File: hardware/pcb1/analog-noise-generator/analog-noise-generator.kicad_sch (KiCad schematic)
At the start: 83 parts, among them J1 USB_C_Receptacle_USB2.0, J2 Conn_01x03_Pin, J3 PJ-211A, J4 PJ-211A, J5 Conn_01x04_Pin, J6 Conn_01x04_Pin, J7 Conn_01x02_Pin, J9 Conn_02x04_Odd_Even, U1 STM32F072CBTx, U2 USBLC6-2SC6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

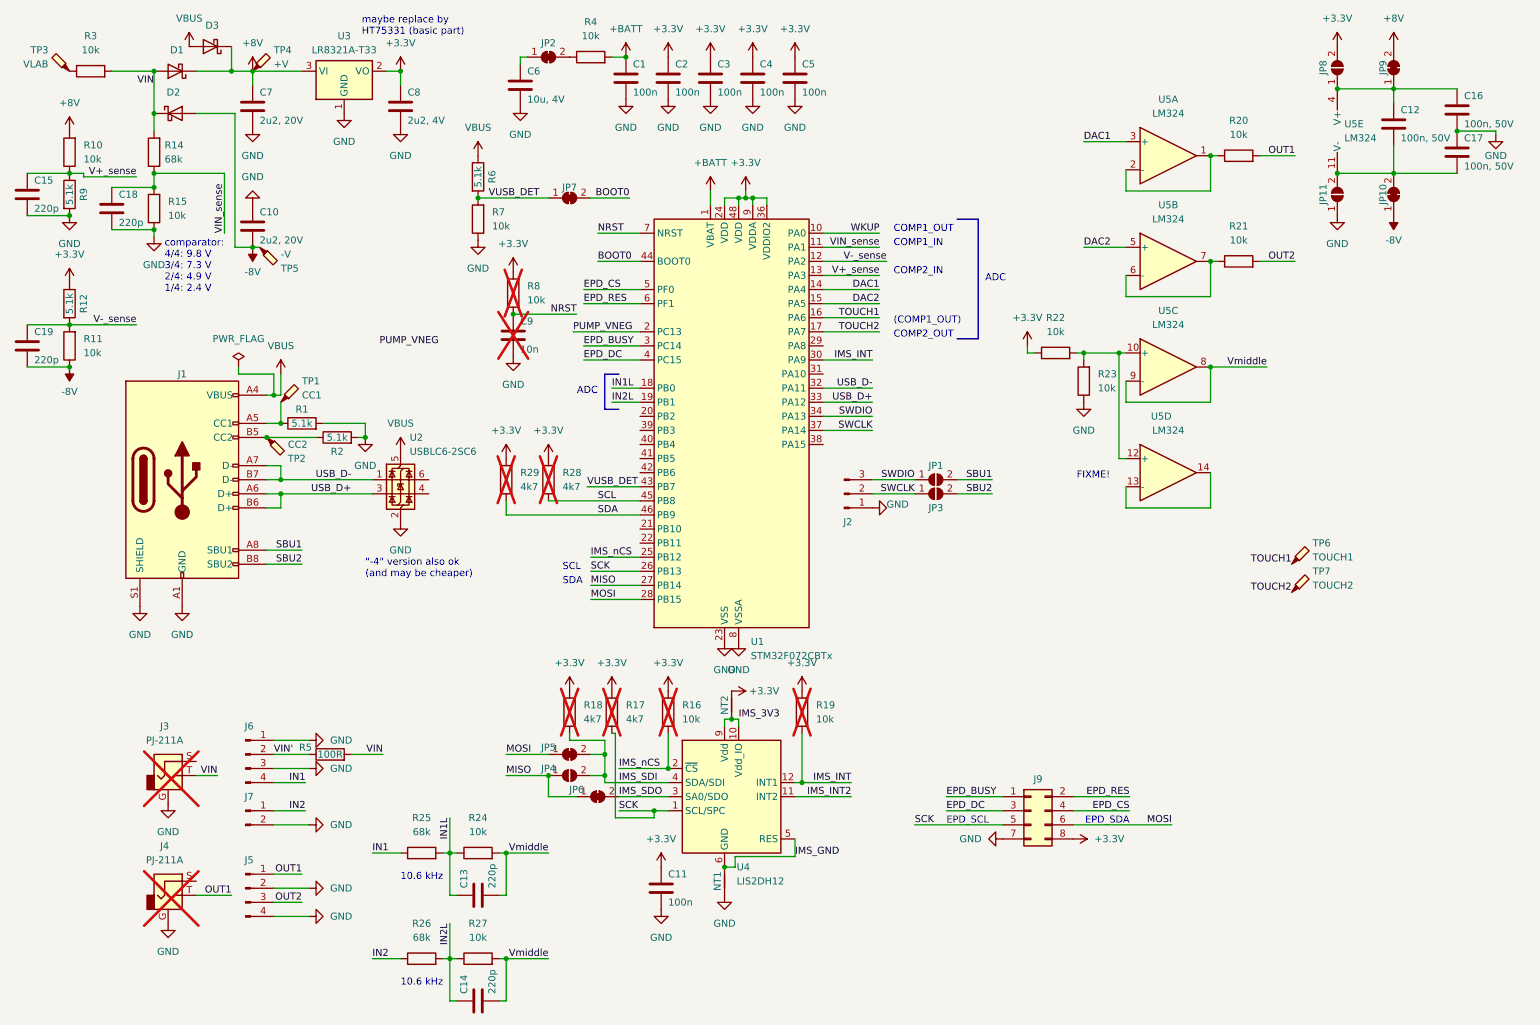
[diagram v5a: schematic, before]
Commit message: remove negative voltage, add more LCSC part numbers, connect opamps
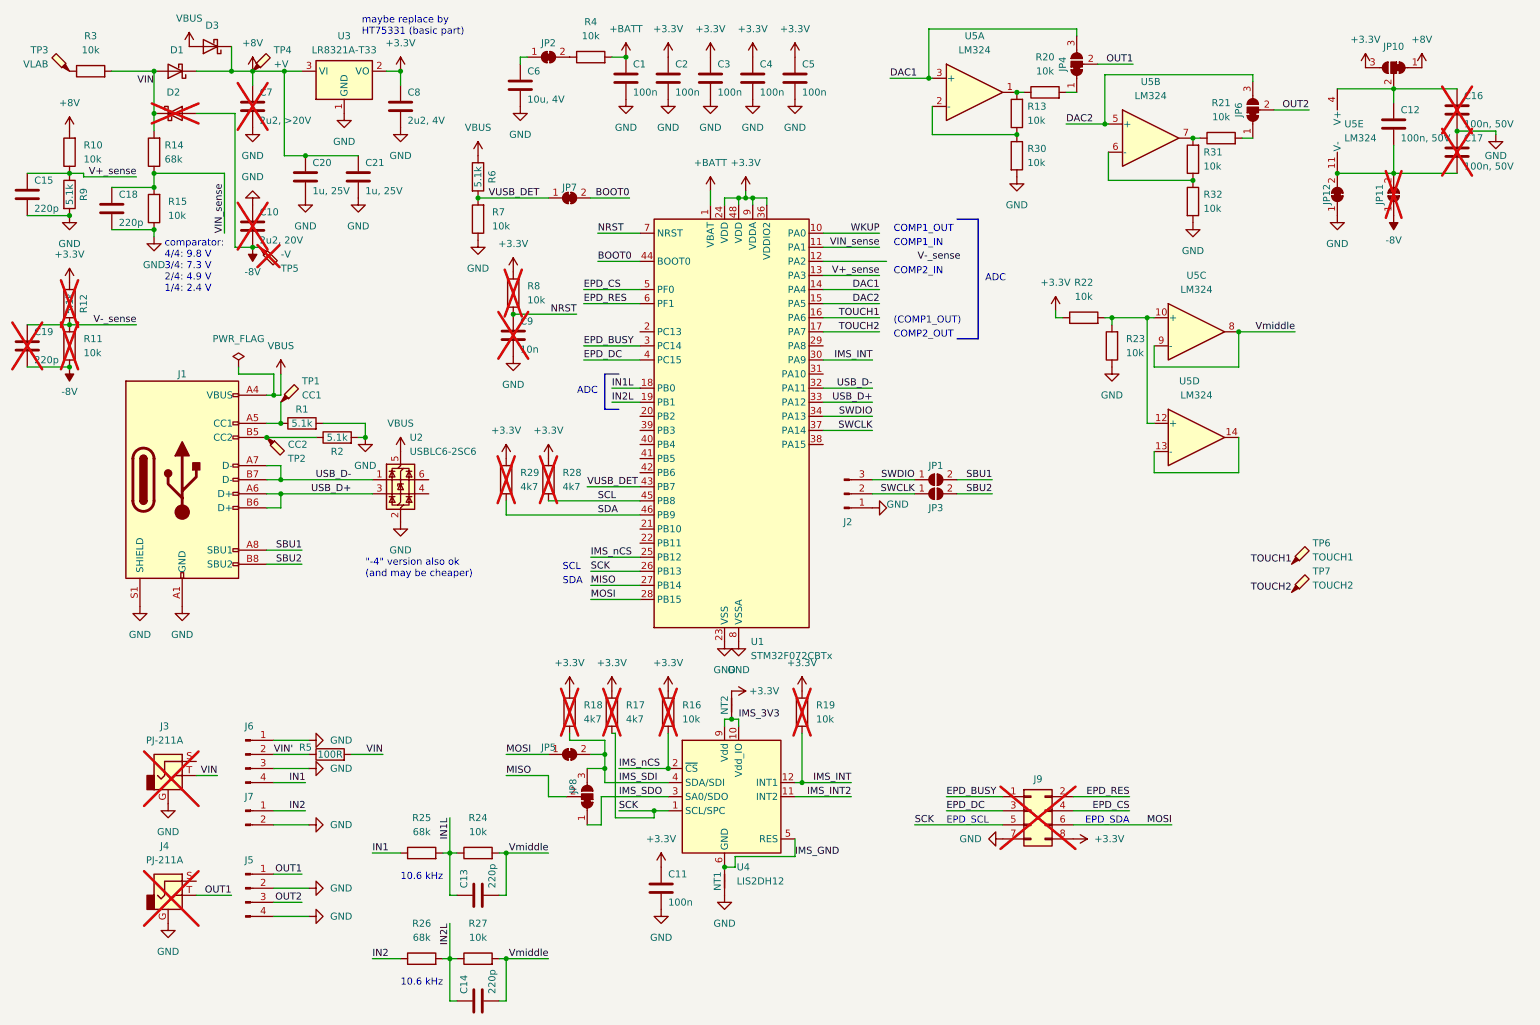
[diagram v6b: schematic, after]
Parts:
- removed JP10, JP6, JP9: SolderJumper_2_Bridged, Jumper:SolderJumper-2_P1.3mm_Bridged_RoundedPad1.0x1.5mm, symbol Jumper:SolderJumper_2_Bridged
- removed JP4, JP8: SolderJumper_2_Open, Jumper:SolderJumper-2_P1.3mm_Open_RoundedPad1.0x1.5mm, symbol Jumper:SolderJumper_2_Open
- added C20, C21: 1u, 25V, Capacitor_SMD:C_0402_1005Metric, symbol Device:C
- added JP10, JP4, JP6, JP8: SolderJumper_3_Bridged12, Jumper:SolderJumper-3_P1.3mm_Bridged12_RoundedPad1.0x1.5mm, symbol Jumper:SolderJumper_3_Bridged12
- added JP12: SolderJumper_2_Bridged, Jumper:SolderJumper-2_P1.3mm_Bridged_RoundedPad1.0x1.5mm, symbol Jumper:SolderJumper_2_Bridged
- added R13, R30, R31, R32: 10k, Resistor_SMD:R_0402_1005Metric, symbol Device:R
- C10: footprint Capacitor_SMD:C_0402_1005Metric -> Capacitor_SMD:C_0805_2012Metric; LCSC (none) -> C377773; now not fitted; now left out of the parts list
- C12: LCSC (none) -> C307331
- C13, C14, C15, C18: LCSC (none) -> C1530
- C16, C17: LCSC (none) -> C307331; now not fitted; now left out of the parts list
- C19: LCSC (none) -> C1530; now not fitted; now left out of the parts list
- C6: LCSC (none) -> C15525
- C7: value 2u2, 20V -> 2u2, >20V; footprint Capacitor_SMD:C_0402_1005Metric -> Capacitor_SMD:C_0805_2012Metric; LCSC (none) -> C377773; now not fitted; now left out of the parts list
- C8: LCSC (none) -> C12530
- C9: LCSC (none) -> C15195
- D2, JP11, R11, R12: now not fitted; now left out of the parts list
- J9, TP5: now not fitted
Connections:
- net +3.3V: now also JP10.3 (B)
- net +8V: now also C20.1, C21.1, JP10.1 (A)
- net -8V: now also JP11.1 (A)
- net DAC1: now also JP4.3 (B)
- net DAC2: now also JP6.3 (B)
- net GND: now also C20.2, C21.2, JP12.1 (A), R30.2, R32.2; no longer JP11.1 (A)
- net IMS_SDI: now also JP8.3 (B)
- net IMS_SDO: now also JP8.1 (A)
- net MISO: now also JP8.2 (C)
- net OUT1: now also JP4.2 (C); no longer R20.2
- net OUT2: now also JP6.2 (C); no longer R21.2
- net V-_sense: no longer U1.12 (PA2)
- net at R21.1, U5.7: now also R31.2; no longer U5.6 (-)
- net at C12.1, C16.1, U5.4 (V+): now also JP10.2 (C)
- net at C12.2, C17.2, JP11.2 (B)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: now also JP12.2 (B)
- net at R20.1, U5.1: now also R13.2; no longer U5.2 (-)
- net PUMP_VNEG: no longer names the net of U1.2 (PC13)
- new net: JP6.1 (A), R21.2
- new net: R31.1, R32.1, U5.6 (-)
- new net: R13.1, R30.1, U5.2 (-)
- new net: JP4.1 (A), R20.2
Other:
- note removed: "FIXME!"
- moved on the sheet: R20, R21, R22, R23, U5A, U5B, U5C, U5D

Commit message: start routing
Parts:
- R10: value 10k -> 20k; LCSC C25744 -> C25765
- TP1, TP2: footprint analog-noise-generator:TestPoint_THTPad_small -> TestPoint:TestPoint_Pad_1.0x1.0mm
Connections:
- net GND: now also C13.2
- net IMS_GND: now also C14.2
- net VIN: no longer R14.2
- net VIN': now also R14.2
- net Vmiddle: no longer C13.2, C14.2
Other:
- note added: "36 kHz"
- note added: "8..800 Hz"
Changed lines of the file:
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@@
 (kicad_sch (version 20230121) (generator eeschema)
   (paper "A4")
+  (junction (at 38.1 22.86) (diameter 0) (color 0 0 0 0)
+  )
   (junction (at 142.24 139.7) (diameter 0) (color 0 0 0 0)
   )
@@
   (junction (at 144.78 45.72) (diameter 0) (color 0 0 0 0)
   )
-  (junction (at 101.6 182.88) (diameter 0) (color 0 0 0 0)
-  )
   (junction (at 217.17 67.31) (diameter 0) (color 0 0 0 0)
   )
-  (junction (at 101.6 163.83) (diameter 0) (color 0 0 0 0)
-  )
   (junction (at 60.96 96.52) (diameter 0) (color 0 0 0 0)
   )
@@
   (junction (at 91.44 163.83) (diameter 0) (color 0 0 0 0)
   )
-  (junction (at 38.1 22.86) (diameter 0) (color 0 0 0 0)
-  )
   (junction (at 233.68 69.85) (diameter 0) (color 0 0 0 0)
   )
-  (junction (at 38.1 30.48) (diameter 0) (color 0 0 0 0)
-  )
   (junction (at 22.86 76.2) (diameter 0) (color 0 0 0 0)
   )
@@
     (stroke (width 0) (type default))
   )
-  (wire (pts (xy 101.6 190.5) (xy 101.6 182.88))
-    (stroke (width 0) (type default))
-  )
   (wire (pts (xy 73.66 146.05) (xy 79.375 146.05))
     (stroke (width 0) (type default))
@@
     (stroke (width 0) (type default))
   )
-  (wire (pts (xy 100.33 182.88) (xy 101.6 182.88))
+  (wire (pts (xy 100.33 182.88) (xy 109.22 182.88))
     (stroke (width 0) (type default))
   )
@@
     (stroke (width 0) (type default))
   )
-  (wire (pts (xy 38.1 30.48) (xy 38.1 33.655))
-    (stroke (width 0) (type default))
-  )
   (wire (pts (xy 182.88 99.06) (xy 189.23 99.06))
     (stroke (width 0) (type default))
@@
     (stroke (width 0) (type default))
   )
-  (wire (pts (xy 100.33 163.83) (xy 101.6 163.83))
-    (stroke (width 0) (type default))
-  )
   (wire (pts (xy 210.185 42.545) (xy 225.425 42.545))
     (stroke (width 0) (type default))
@@
     (stroke (width 0) (type default))
   )
-  (wire (pts (xy 101.6 171.45) (xy 101.6 163.83))
-    (stroke (width 0) (type default))
-  )
   (wire (pts (xy 234.315 34.925) (xy 236.22 34.925))
     (stroke (width 0) (type default))
@@
     (stroke (width 0) (type default))
   )
-  (wire (pts (xy 101.6 182.88) (xy 109.22 182.88))
-    (stroke (width 0) (type default))
-  )
   (wire (pts (xy 210.82 67.31) (xy 217.17 67.31))
     (stroke (width 0) (type default))
@@
     (stroke (width 0) (type default))
   )
+  (wire (pts (xy 38.1 22.86) (xy 38.1 30.48))
+    (stroke (width 0) (type default))
+  )
   (wire (pts (xy 167.64 96.52) (xy 175.26 96.52))
     (stroke (width 0) (type default))
@@
     (stroke (width 0) (type default))
   )
-  (wire (pts (xy 101.6 163.83) (xy 109.22 163.83))
+  (wire (pts (xy 100.33 163.83) (xy 109.22 163.83))
     (stroke (width 0) (type default))
   )
@@
     (stroke (width 0) (type default))
   )
-  (wire (pts (xy 100.33 190.5) (xy 101.6 190.5))
+  (wire (pts (xy 100.33 190.5) (xy 110.49 190.5))
     (stroke (width 0) (type default))
   )
@@
     (stroke (width 0) (type default))
   )
-  (wire (pts (xy 38.1 22.86) (xy 38.1 30.48))
-    (stroke (width 0) (type default))
-  )
   (wire (pts (xy 140.97 139.7) (xy 142.24 139.7))
     (stroke (width 0) (type default))
@@
     (stroke (width 0) (type default))
   )
+  (wire (pts (xy 33.02 33.655) (xy 38.1 33.655))
+    (stroke (width 0) (type default))
+  )
   (polyline (pts (xy 182.88 49.53) (xy 186.69 49.53))
     (stroke (width 0) (type default))
@@
     (effects (font (size 1.27 1.27)) (justify left bottom))
   )
+  (text "10.6 kHz" (at 40.64 64.77 0)
+    (effects (font (size 1.27 1.27)) (justify left bottom))
+  )
   (text "(COMP1_OUT)" (at 171.45 68.58 0)
     (effects (font (size 1.27 1.27)) (justify left bottom))
@@
     (effects (font (size 1.27 1.27)) (justify left bottom))
   )
+  (text "36 kHz" (at 12.7 40.64 0)
+    (effects (font (size 1.27 1.27)) (justify left bottom))
+  )
   (text "EPD_SDA" (at 213.995 158.75 0)
     (effects (font (size 1.27 1.27)) (justify right bottom))
   )
+  (text "8..800 Hz" (at 78.74 48.26 0)
+    (effects (font (size 1.27 1.27)) (justify left bottom))
+  )
   (text "ADC" (at 118.11 81.28 0)
     (effects (font (size 1.27 1.27)) (justify right bottom))
@@
     (effects (font (size 1.27 1.27)) (justify left bottom))
   )
-  (label "VIN" (at 38.1 25.4 180) (fields_autoplaced)
+  (label "VIN" (at 36.83 22.86 180) (fields_autoplaced)
     (effects (font (size 1.27 1.27)) (justify right bottom))
   )
@@
     (effects (font (size 1.27 1.27)) (justify left bottom))
   )
+  (label "VIN'" (at 33.02 33.655 0) (fields_autoplaced)
+    (effects (font (size 1.27 1.27)) (justify left bottom))
+  )
   (label "BOOT0" (at 123.825 45.72 180) (fields_autoplaced)
     (effects (font (size 1.27 1.27)) (justify right bottom))
@@
     (effects (font (size 1.27 1.27)) (justify right bottom))
   )
+  (label "IMS_GND" (at 110.49 190.5 180) (fields_autoplaced)
+    (effects (font (size 1.27 1.27)) (justify right bottom))
+  )
   (label "VIN'" (at 59.69 146.05 0) (fields_autoplaced)
     (effects (font (size 1.27 1.27)) (justify left bottom))
@@
       (effects (font (size 1.27 1.27)) (justify right))
     )
-    (property "Value" "10k" (at 25.4 38.735 0)
+    (property "Value" "20k" (at 25.4 38.735 0)
       (effects (font (size 1.27 1.27)) (justify right))
     )
@@
       (effects (font (size 1.27 1.27)) hide)
     )
-    (property "LCSC" "C25744" (at 22.86 37.465 0)
+    (property "LCSC" "C25765" (at 22.86 37.465 0)
       (effects (font (size 1.27 1.27)) hide)
     )
@@
       (effects (font (size 1.27 1.27)) (justify left))
     )
-    (property "Footprint" "analog-noise-generator:TestPoint_THTPad_small" (at 66.04 82.55 0)
+    (property "Footprint" "TestPoint:TestPoint_Pad_1.0x1.0mm" (at 66.04 82.55 0)
       (effects (font (size 1.27 1.27)) hide)
     )
@@
     )
   )
+  (symbol (lib_id "power:GND") (at 101.6 171.45 90) (unit 1)
+    (in_bom yes) (on_board yes) (dnp no) (fields_autoplaced)
+    (property "Reference" "#PWR071" (at 107.95 171.45 0)
+      (effects (font (size 1.27 1.27)) hide)
+    )
+    (property "Value" "GND" (at 105.41 171.45 90)
+      (effects (font (size 1.27 1.27)) (justify right))
+    )
+    (property "Footprint" "" (at 101.6 171.45 0)
+      (effects (font (size 1.27 1.27)) hide)
+    )
+    (property "Datasheet" "" (at 101.6 171.45 0)
+      (effects (font (size 1.27 1.27)) hide)
+    )
+    (pin "1")
+    (instances
+      (project "analog-noise-generator"
+        (path "/e71fa5ad-0f80-45ec-aa84-70ffc489027a"
+          (reference "#PWR071") (unit 1)
+        )
+      )
+    )
+  )
   (symbol (lib_id "Device:R") (at 22.86 72.39 180) (unit 1)
     (in_bom no) (on_board no) (dnp yes) (fields_autoplaced)
@@
       (effects (font (size 1.27 1.27)) (justify left))
     )
-    (property "Footprint" "analog-noise-generator:TestPoint_THTPad_small" (at 63.5 88.9 0)
+    (property "Footprint" "TestPoint:TestPoint_Pad_1.0x1.0mm" (at 63.5 88.9 0)
       (effects (font (size 1.27 1.27)) hide)
     )
